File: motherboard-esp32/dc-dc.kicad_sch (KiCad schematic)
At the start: 0 parts

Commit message: proof of concept
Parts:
- added C1: 0.1u, bio-robot:C_0603_1608Metric, symbol bio-robot:C_0.1u
- added C10: 1nF, bio-robot:C_0603_1608Metric, symbol bio-robot:C_1nF
- added C11: 3.3nF, bio-robot:C_0603_1608Metric, symbol bio-robot:C_3.3nF
- added C12: 47uF, bio-robot:CAP_EEEFT1H470AP, symbol bio-robot:Cpol_EEEFT1H470AP
- added C2: 25SVPF100M, bio-robot:CAP_25SVPF100M, symbol bio-robot:25SVPF100M
- added C3: 10u, bio-robot:C_0805_2012Metric, symbol bio-robot:C_10u
- added C4: 30p, bio-robot:C_0603_1608Metric, symbol bio-robot:C_30p
- added C5: 2.2u, bio-robot:C_0805_2012Metric, symbol bio-robot:C_2.2u_0805
- added C6: 16SVPF180M, bio-robot:CAP_16SVPF180M, symbol bio-robot:16SVPF180M
- added C7, C8: 22u_1206, bots:C_1206_3216Metric, symbol bots:C_22u_1206
- added C9: 0.47u, bio-robot:C_0603_1608Metric, symbol bio-robot:C_0.47u
- added D2: STPS20M100SG-TR, bio-robot:TO-263-2, symbol bio-robot:D_STPS20M100SG-TR
- added L1: 27uH, bio-robot:IND_CDRH127_LDNP-470MC_SUM, symbol bio-robot:CDRH127/LDNP-220MC
- added L2: 3.3uH, bio-robot:IND_MDA1050-3R3M, symbol bio-robot:L_MDA1050-3R3M
- added Q3: DOD4185, bio-robot:DPAK-3_ONS, symbol bio-robot:Q_Pch40V45A
- added R3: 113k, bio-robot:R_0603_1608Metric, symbol bio-robot:R_113k
- added R4: 4.12k, bio-robot:R_0603_1608Metric, symbol bio-robot:R_4.12k
- added R5: 10m, bio-robot:R_0805_2012Metric, symbol bio-robot:R_10m_0805
- added R6: 88.7k, bio-robot:R_0603_1608Metric, symbol bio-robot:R_88.7k
- added R7: 22.1k, bio-robot:R_0603_1608Metric, symbol bio-robot:R_22.1k
- added R8: 10k, bio-robot:R_0603_1608Metric, symbol bio-robot:R_10k
- added R9: 2.26k, bio-robot:R_0603_1608Metric, symbol bio-robot:R_2.26k
- added U1: LMR23630AFDDAR, bio-robot:TI_SO-PowerPAD-8_ThermalVias, symbol bio-robot:LMR23630AFDDAR
- added U2: LM25085MY/NOPB, bio-robot:MSOP8_PowerPad, symbol bio-robot:LM25085MY_NOPB
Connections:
- new net +5V: C4.1, C6.1, L1.1, R6.1
- new net +6.8V: C11.1, C12.1, L2.1, R8.1
- new net ADJ: C10.1, R4.1, U2.1 (ADJ)
- new net BOOT: C1.1, U1.2 (BOOT)
- new net CVCC: C9.2, U2.7 (VCC)
- new net FB: C4.2, R6.2, R7.1, U1.4 (FB)
- new net FB1: C11.2, R8.2, R9.1, U2.3 (FB)
- new net GND: C12.2, C2.2, C3.2, C5.2, C6.2, C7.2, C8.2, D2.2 (A), R7.2, R9.2, U1.6 (AGND), U1.8 (PGND), U1.9 (PAD), U2.4 (GND), U2.9 (EP)
- new net ISEN: Q3.3 (S), R5.2, U2.5 (ISEN)
- new net LM_OUT: C1.2, L1.2, U1.1 (SW)
- new net LOUT: D2.1 (K), L2.2, Q3.2 (D)
- new net PGATE: Q3.1 (G), U2.6 (PGATE)
- new net RT: R3.2, U2.2 (RT)
- new net U1_VCC: C5.1, U1.3 (VCC)
- new net VCC: C10.2, C2.1, C3.1, C7.1, C8.1, C9.1, R3.1, R4.2, R5.1, U1.5 (EN/SYNC), U1.7 (VIN), U2.8 (VIN)
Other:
- note added: "5V 3A buck converter for Raspberry Pi boards (for other projects)"
- note added: "variable input to 6.8V / 10A output"
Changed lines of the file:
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@@
 	(generator_version "9.0")
 	(paper "A4")
-)

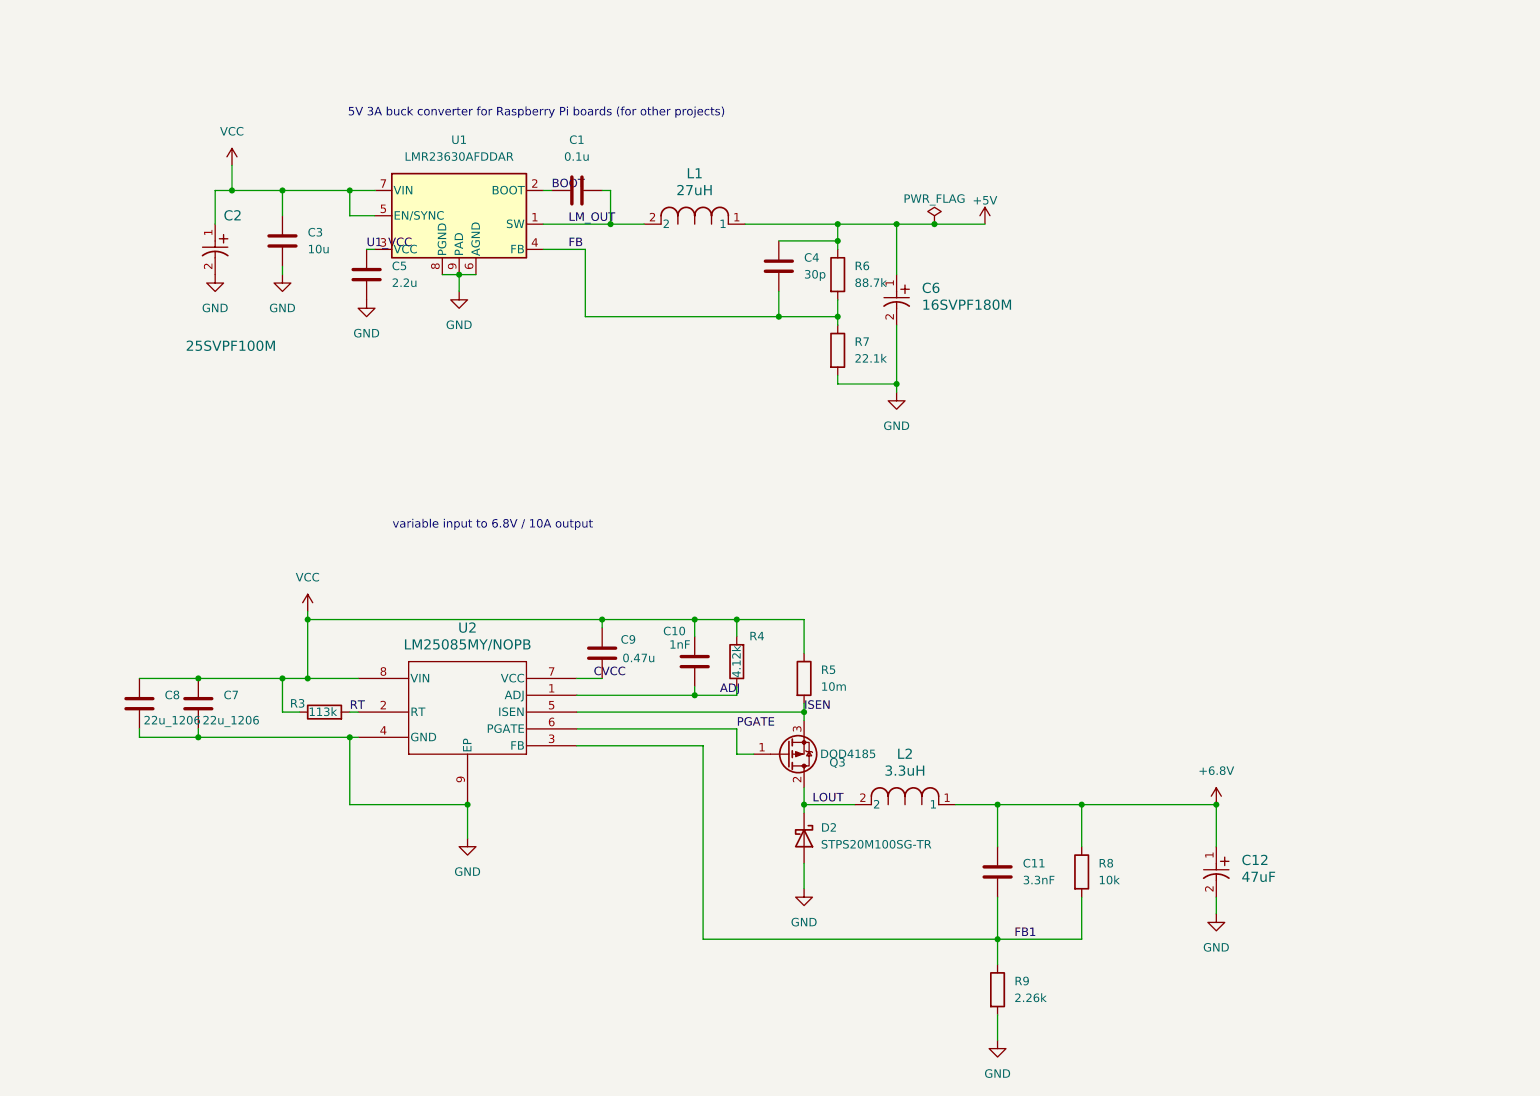
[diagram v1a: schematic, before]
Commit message: split into two boards for dc/dc converter
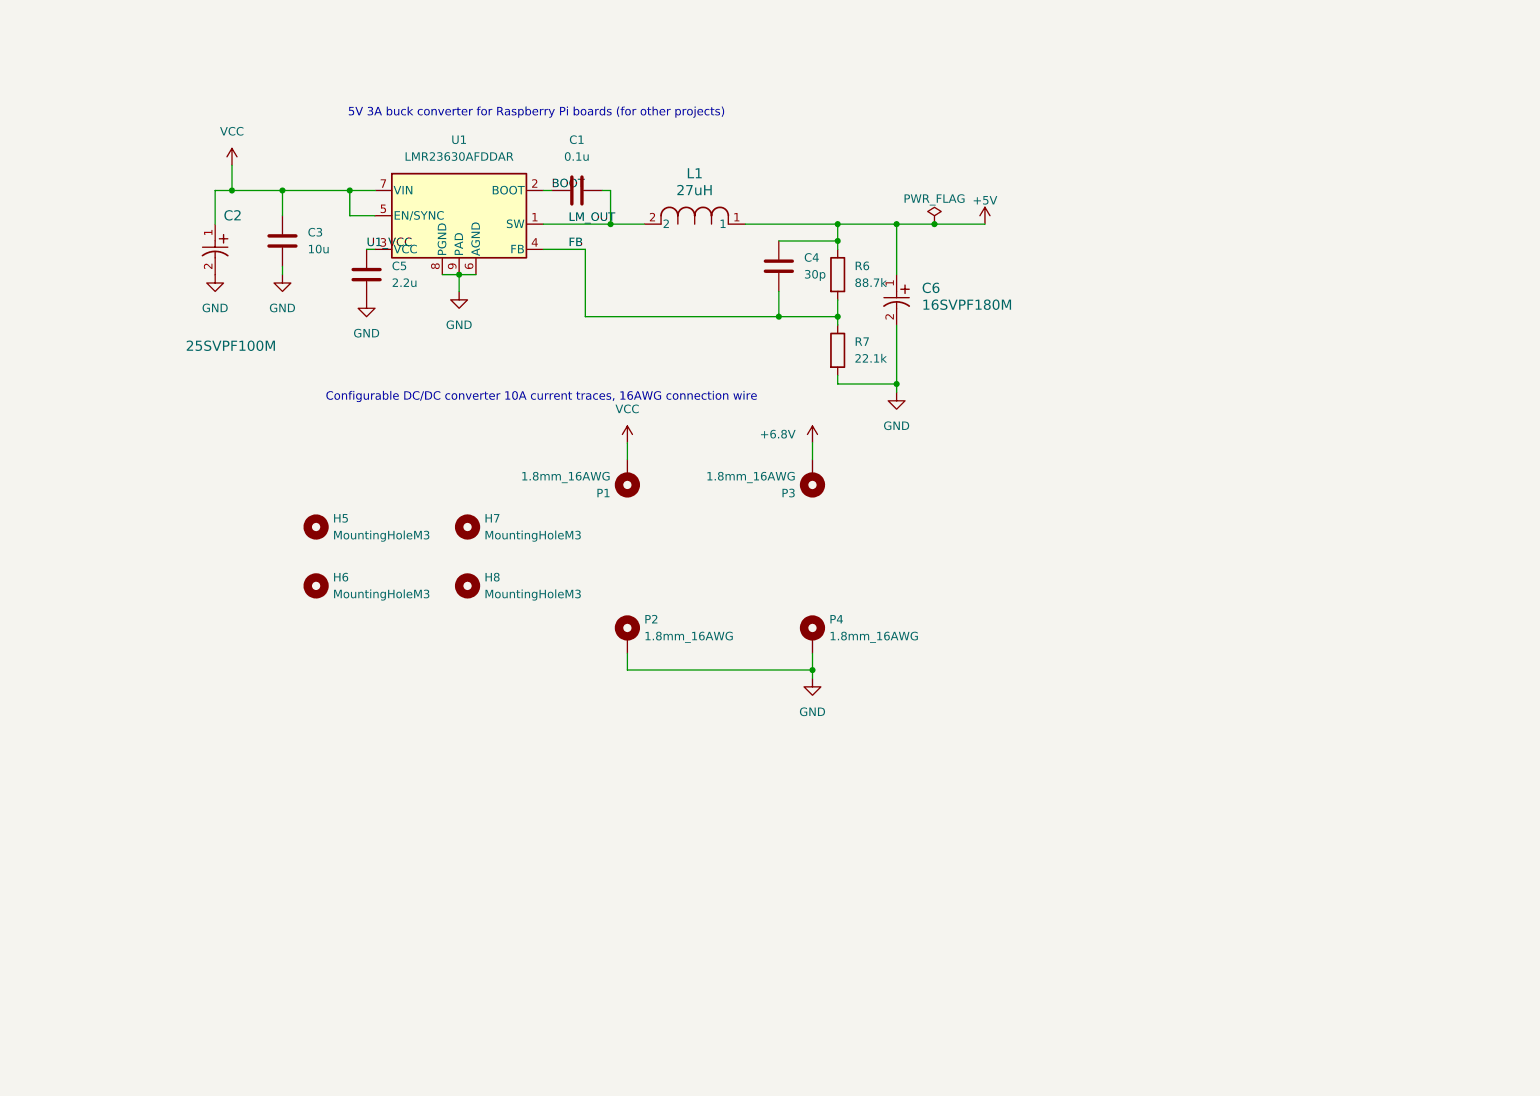
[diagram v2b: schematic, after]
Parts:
- removed C10: 1nF, bio-robot:C_0603_1608Metric, symbol bio-robot:C_1nF
- removed C11: 3.3nF, bio-robot:C_0603_1608Metric, symbol bio-robot:C_3.3nF
- removed C12: 47uF, bio-robot:CAP_EEEFT1H470AP, symbol bio-robot:Cpol_EEEFT1H470AP
- removed C7, C8: 22u_1206, bots:C_1206_3216Metric, symbol bots:C_22u_1206
- removed C9: 0.47u, bio-robot:C_0603_1608Metric, symbol bio-robot:C_0.47u
- removed D2: STPS20M100SG-TR, bio-robot:TO-263-2, symbol bio-robot:D_STPS20M100SG-TR
- removed L2: 3.3uH, bio-robot:IND_MDA1050-3R3M, symbol bio-robot:L_MDA1050-3R3M
- removed Q3: DOD4185, bio-robot:DPAK-3_ONS, symbol bio-robot:Q_Pch40V45A
- removed R3: 113k, bio-robot:R_0603_1608Metric, symbol bio-robot:R_113k
- removed R4: 4.12k, bio-robot:R_0603_1608Metric, symbol bio-robot:R_4.12k
- removed R5: 10m, bio-robot:R_0805_2012Metric, symbol bio-robot:R_10m_0805
- removed R8: 10k, bio-robot:R_0603_1608Metric, symbol bio-robot:R_10k
- removed R9: 2.26k, bio-robot:R_0603_1608Metric, symbol bio-robot:R_2.26k
- removed U2: LM25085MY/NOPB, bio-robot:MSOP8_PowerPad, symbol bio-robot:LM25085MY_NOPB
- added H5, H6, H7, H8: MountingHoleM3, MountingHole:MountingHole_3.2mm_M3_DIN965_Pad, symbol bio-robot:MountingHoleM3
- added P1, P2, P3, P4: 1.8mm_16AWG, bio-robot:SolderPad_TH_16AWG_1.8mm, symbol bio-robot:Solder_Pad 1.8mm 16AWG 10A
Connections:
- net +6.8V: now also P3.1
- net GND: now also P2.1, P4.1
- net VCC: now also P1.1
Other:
- note added: "Configurable DC/DC converter 10A current traces, 16AWG connection wire"
- note removed: "variable input to 6.8V / 10A output"

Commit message: update
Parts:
- added J2, J5, J6: Screw_Terminal_01x02, bio-robot:TerminalBlock_MaiXu_MX126-5.0-02P_1x02_P5.00mm, symbol bio-robot:Screw_Terminal_01x02
- H5, H6, H7, H8: footprint MountingHole:MountingHole_3.2mm_M3_DIN965_Pad -> bio-robot:MountingHole_3.2mm_M3_DIN965_Pad
- renumbered C2 to C1, C3 to C2, C5 to C3, C1 to C4, C4 to C5, R6 to R5, R7 to R6
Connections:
- net +5V: now also J2.1 (Pin_1)
- net +6.8V: now also J5.1 (Pin_1)
- net GND: now also J2.2 (Pin_2); no longer P2.1, P4.1
- net VCC: now also J6.1 (Pin_1); no longer C1.1, C2.1, U1.5 (EN/SYNC), U1.7 (VIN)
- new net +BATT: C1.1, C2.1, U1.5 (EN/SYNC), U1.7 (VIN)
- new net GNDPWR: J5.2 (Pin_2), J6.2 (Pin_2), P2.1, P4.1
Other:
- note added: "5V 3A buck converter"
- note added: "for Raspberry Pi boards (for other projects)"
- note removed: "5V 3A buck converter for Raspberry Pi boards (for other projects)"
- moved on the sheet: C1, C2, C3, C4, C5, C6, L1, P1, P2, P3, P4, R5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

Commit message: update
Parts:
- C6: JLC (none) -> SMD,D6.3xL5.9mm; LCSC (none) -> C136277
- L1: LCSC (none) -> C167262; MPN (none) -> CDRH127/LDNP-220MC
- R5: LCSC C23061 -> C23258; MPN 0603WAF4752T5E -> 0603WAF8872T5E
- R6: LCSC C23061 -> C137768; MPN 0603WAF4752T5E -> RC0603FR-0722K1L; Manufacturer UNI-ROYAL(Uniroyal Elec) -> YAGEO
- U1: JLC (none) -> SO-8; LCSC (none) -> C601653; MPN (none) -> LMR23630AFDDAR
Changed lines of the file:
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@@
+			)
+		)
+		(property "LCSC" "C136277"
+			(at 148.59 55.88 0)
+			(hide yes)
+			(show_name no)
+			(do_not_autoplace no)
+			(effects
+				(font
+					(size 1.27 1.27)
+				)
+			)
+		)
+		(property "JLC" "SMD,D6.3xL5.9mm "
+			(at 148.59 55.88 0)
+			(hide yes)
+			(show_name no)
+			(do_not_autoplace no)
+			(effects
+				(font
+					(size 1.27 1.27)
+				)
 			)
 		)
@@
 			)
 		)
+		(property "MPN" "CDRH127/LDNP-220MC"
+			(at 110.49 48.26 0)
+			(hide yes)
+			(show_name no)
+			(do_not_autoplace no)
+			(effects
+				(font
+					(size 1.27 1.27)
+				)
+			)
+		)
+		(property "LCSC" "C167262"
+			(at 110.49 48.26 0)
+			(hide yes)
+			(show_name no)
+			(do_not_autoplace no)
+			(effects
+				(font
+					(size 1.27 1.27)
+				)
+			)
+		)
 		(pin "1"
 		)
@@
 			)
 		)
-		(property "Description" "Power symbol creates a global label with name \"+6.8V\""
+		(property "Description" "Power symbol creates a global label with name \"+6V\""
 			(at 210.82 106.68 0)
 			(hide yes)
@@
 			)
 		)
-		(property "MPN" "0603WAF4752T5E"
+		(property "MPN" "RC0603FR-0722K1L"
 			(at 139.7 67.31 0)
 			(hide yes)
@@
 			)
 		)
-		(property "Manufacturer" "UNI-ROYAL(Uniroyal Elec)"
+		(property "Manufacturer" "YAGEO"
 			(at 139.7 67.31 0)
 			(hide yes)
@@
 			)
 		)
-		(property "LCSC" "C23061"
+		(property "LCSC" "C137768"
 			(at 139.7 67.31 0)
 			(hide yes)
@@
 			)
 		)
-		(property "Description" "Power symbol creates a global label with name \"+6.8V\""
+		(property "Description" "Power symbol creates a global label with name \"+6V\""
 			(at 144.78 100.33 0)
 			(hide yes)
@@
 			)
 		)
+		(property "LCSC" "C601653"
+			(at 82.55 48.26 0)
+			(hide yes)
+			(show_name no)
+			(do_not_autoplace no)
+			(effects
+				(font
+					(size 1.27 1.27)
+				)
+			)
+		)
+		(property "MPN" "LMR23630AFDDAR"
+			(at 82.55 48.26 0)
+			(hide yes)
+			(show_name no)
+			(do_not_autoplace no)
+			(effects
+				(font
+					(size 1.27 1.27)
+				)
+			)
+		)
+		(property "JLC" "SO-8"
+			(at 82.55 48.26 0)
+			(hide yes)
+			(show_name no)
+			(do_not_autoplace no)
+			(effects
+				(font
+					(size 1.27 1.27)
+				)
+			)
+		)
 		(pin "1"
 		)
@@
 			)
 		)
-		(property "MPN" "0603WAF4752T5E"
+		(property "MPN" "0603WAF8872T5E"
 			(at 139.7 55.88 0)
 			(hide yes)
@@
 			)
 		)
-		(property "LCSC" "C23061"
+		(property "LCSC" "C23258"
 			(at 139.7 55.88 0)
 			(hide yes)
@@
 		)
 	)
-	(group "5V 3A Buck Converter"
-		(lib_id "design-block:5V 3A Buck Converter")
-		(members "00bd5588-fc4f-4886-b1d0-c6878c2c6e5f" "01a324bc-0e3d-44c2-8785-f31c1a2df417"
-			"05c4bdfd-92a1-4b01-a9fb-96dd1d33adec" "06121eac-75a2-4520-bed5-4f125f3de31e"
-			"062f0849-7912-43ea-9035-92916df6ace8" "0f8edf2a-23d4-4bae-a8bd-a250cb78da08"
-			"0fd6108a-1cae-4a7f-a061-b9c858b124fa" "14e30c31-08aa-414b-9c97-e0906d3c0dcb"
-			"24100b78-cab9-4066-b07d-56fd4d2802ba" "2f133d40-5ae2-460d-8a35-0e4c165f94aa"
-			"2f425d2b-d105-4871-b872-e713798c8908" "3302f42b-6179-4dc1-86f6-5abb1ed005be"
-			"33ac2d7d-8225-4af2-80c8-cbbb59f1da4f" "3411bb11-e06b-497b-a965-0113f1d3320b"
-			"35c6da0c-d9f7-40e2-bef4-c6401e99533c" "3d9c9324-2515-437c-a8c3-58ae5792d233"
-			"416741de-4b8e-4287-8914-7c18140ae61b" "42151860-a5a4-41de-8000-ff35535f6092"
-			"435d1b0f-c8d8-466a-b313-d1b887514fcd" "467a7723-2c6f-4c7a-9ada-da9500f04902"
-			"487e6c62-ae6d-47c3-a8a7-3d798a3ea529" "4ee49fa1-fcb7-45d9-95f3-a397a5e0ed25"
-			"50dc41f8-c2e2-4bc6-b13a-f9458cfc8eef" "52db5f26-8656-4327-bd01-6ce0a7687232"
-			"5d4d16fc-8cb1-4ee1-9f3b-3a03ca9db76f" "654ea281-f988-4cb1-92ce-415cd3d58c92"
-			"659cedd7-8489-4ad2-b0a6-6b9ca81e3c50" "6877b07a-8489-4ec3-9ffb-2a3aab6ce4c1"
-			"69d72c95-cb37-4b7e-9982-439b3536a789" "6f12ad7e-69b9-4638-b66b-eb7c23f73bc2"
-			"71328c46-006d-46d8-a576-8d76ea34eec4" "752cbef7-347f-4cdc-9ce2-d3b5b0be9b5c"
-			"758e8236-0405-4752-936b-77ed2ca5a2c0" "76b3611a-a33b-45e0-995a-d0352f495e8f"
-			"7b0940c8-dca0-4885-a10a-a5f2f2699f73" "7bfa6647-9c30-4375-8a7e-42fa2a29936a"
-			"7d4c9cb2-561b-4caf-897e-b87a568fe6af" "7ecb239b-a9f8-4927-a3fb-41b0905f36c7"
-			"8351bc90-eff7-44dd-a52b-2455077a6884" "844aef78-13ed-4fb0-9419-3af12cc48540"
-			"851286a3-f903-4a1b-b98c-58ae624c3b41" "859635dc-fc9c-4059-915a-318786cb4a7d"
-			"8b588c3a-baf7-4ffe-83c2-8db50eabcad7" "8c397448-899c-407e-8201-9f7fb2ac0e7a"
-			"8ee33ab0-063c-46ca-bc54-7505e845f970" "9ab4511a-ddd1-4234-8532-0368144678f1"
-			"9fa7a82c-b72b-436d-ac03-00dac254dc39" "9ff7ea17-c544-4c30-aa28-554c70ee5199"
-			"af515fd6-f00c-48fc-be49-b5528efad9f5" "b128f005-8a4d-4d12-8e28-33160c4996dd"
-			"b1f81039-33fb-4067-b8a5-781e99a41ce2" "b7cde8f2-dd0f-4ea5-9e49-9992fb0a5cc2"
-			"bbf73491-7d88-460c-a9b9-8e6236c37c44" "bf6d74ee-045f-4aa4-bb79-de5edf854690"
-			"c74e64b4-65a5-4f61-8886-2c0612877dfa" "c943cc66-d545-4b97-9e4d-49ef55e3e5ac"
-			"cb3f140c-cb29-4fdc-9d4a-6d7a03c71f68" "cd49f865-2469-478f-86af-4f3c5224264a"
-			"cd92f93c-75b4-42fb-8cfe-a723b8d98600" "ce83cbce-e5e9-4f63-8f37-7f8cd2cee151"
-			"cfdb2080-47ad-4b08-96bf-42787d36fd83" "d00877f7-6523-45e0-b1b2-ddc4d1a138f1"
-			"d25d0572-c08e-4039-8262-03707de81bbe" "d3d50dbd-694d-45b7-bb66-a116b39d9737"
-			"d4b34a25-3002-4dfd-b17a-0f49d1f05008" "d8761522-f0b6-45ed-a2e4-0e8c08fcbd2b"
-			"dbcf2dad-dfaa-4292-8628-76d26babb636" "e1773c38-0329-4ef9-b159-c902fd661ceb"
-			"ec5ed6fd-79b0-4bbf-b5f4-257754b8844e" "ed96274a-9408-4cee-a5ae-2ee0ef8f60db"
-			"eea29928-fae5-41e1-b21d-a7f995963999" "f82fc692-b69a-4ef1-899c-248fb7f6a9a2"
-			"f8a55b6b-a58d-4675-9489-28fe96ddc293" "fc7bf563-8f9c-4807-aa59-123fb3c41f95"
-			"fcc2161b-ff1f-4e46-8147-59bd16ca5fe1"
-		)
-	)

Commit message: 5V 5A version
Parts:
- removed C1: 25SVPF100M, bio-robot:CAP_25SVPF100M, symbol bio-robot:25SVPF100M
- removed C2: 10u, bio-robot:C_0805_2012Metric, symbol bio-robot:C_10u
- removed C3: 2.2u, bio-robot:C_0805_2012Metric, symbol bio-robot:C_2.2u_0805
- removed C5: 30p, bio-robot:C_0603_1608Metric, symbol bio-robot:C_30p
- removed C6: 16SVPF180M, bio-robot:CAP_16SVPF180M, symbol bio-robot:16SVPF180M
- removed L1: 27uH, bio-robot:IND_CDRH127_LDNP-470MC_SUM, symbol bio-robot:CDRH127/LDNP-220MC
- removed R5: 88.7k, bio-robot:R_0603_1608Metric, symbol bio-robot:R_88.7k
- removed R6: 22.1k, bio-robot:R_0603_1608Metric, symbol bio-robot:R_22.1k
- removed U1: LMR23630AFDDAR, bio-robot:TI_SO-PowerPAD-8_ThermalVias, symbol bio-robot:LMR23630AFDDAR
- added C1: 22u_1206, bio-robot:C_1206_3216Metric, symbol bio-robot:C_22u_1206
- added C2: 10SVPC120M, bio-robot:CAP_10SVPC120MV, symbol bio-robot:Cpol_10SVPC120M
- added C7, C9: 10u, bio-robot:C_0805_2012Metric, symbol bio-robot:C_10u
- added C8: 0.1u, bio-robot:C_0603_1608Metric, symbol bio-robot:C_0.1u
- added H10, H9: MountingHoleM3, bio-robot:MountingHole_3.2mm_M3_DIN965_Pad, symbol bio-robot:MountingHoleM3
- added L1: 4.7u, bio-robot:IND_XAL6060-472MEC, symbol bio-robot:L_XAL6060-472MEB
- added R12: 698k, bio-robot:R_0603_1608Metric, symbol bio-robot:R_698k
- added R13: 30.9k, bio-robot:R_0603_1608Metric, symbol bio-robot:R_30.9k
- added R14: 200k, bots:R_0603_1608Metric, symbol bots:R_200k
- added R15, R5: 100k, bots:R_0603_1608Metric, symbol bio-robot:R_100k
- added R6: 19.1k, bio-robot:R_0603_1608Metric, symbol bio-robot:R_19.1k
- added U2: LMR51450SDRRR, bio-robot:CONV_LMR51450SDRRR, symbol bio-robot:LMR51450SDRRR
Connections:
- net +5V: now also C1.1, C2.1, L1.1, R15.2, R5.2
- net +BATT: now also C7.1, C8.2, C9.1, R12.1, U2.10 (VIN), U2.11 (VIN), U2.12 (VIN)
- net BOOT: now also U2.4 (BOOT)
- net FB: now also R5.1, R6.1, U2.7 (FB)
- net GND: now also C1.2, C2.2, C7.2, C8.1, C9.2, R13.2, R14.2, R6.2, U2.13 (PGND), U2.8 (AGND)
- net LM_OUT: now also L1.2, U2.1 (SW), U2.2 (SW), U2.3 (SW)
- new net EN: R12.2, R14.1, U2.9 (EN)
- new net PG: R15.1, U2.5 (PG)
- new net RT: R13.1, U2.6 (RT)
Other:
- note added: "5V 5A buck converter"
- note removed: "5V 3A buck converter"
- moved on the sheet: C4
